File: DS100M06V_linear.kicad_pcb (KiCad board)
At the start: 4 copper layers, 100 x 60 mm, 134 parts, among them J1 wire2board, J10 BNC_panel_mount, J11 wire2board, J2 Wire2Board, J3 wire2board, J4 wire2board, J5 Wire2Board, J6 Wire2Board, J7 Wire2Board, J8 red_safety_4mm_connector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

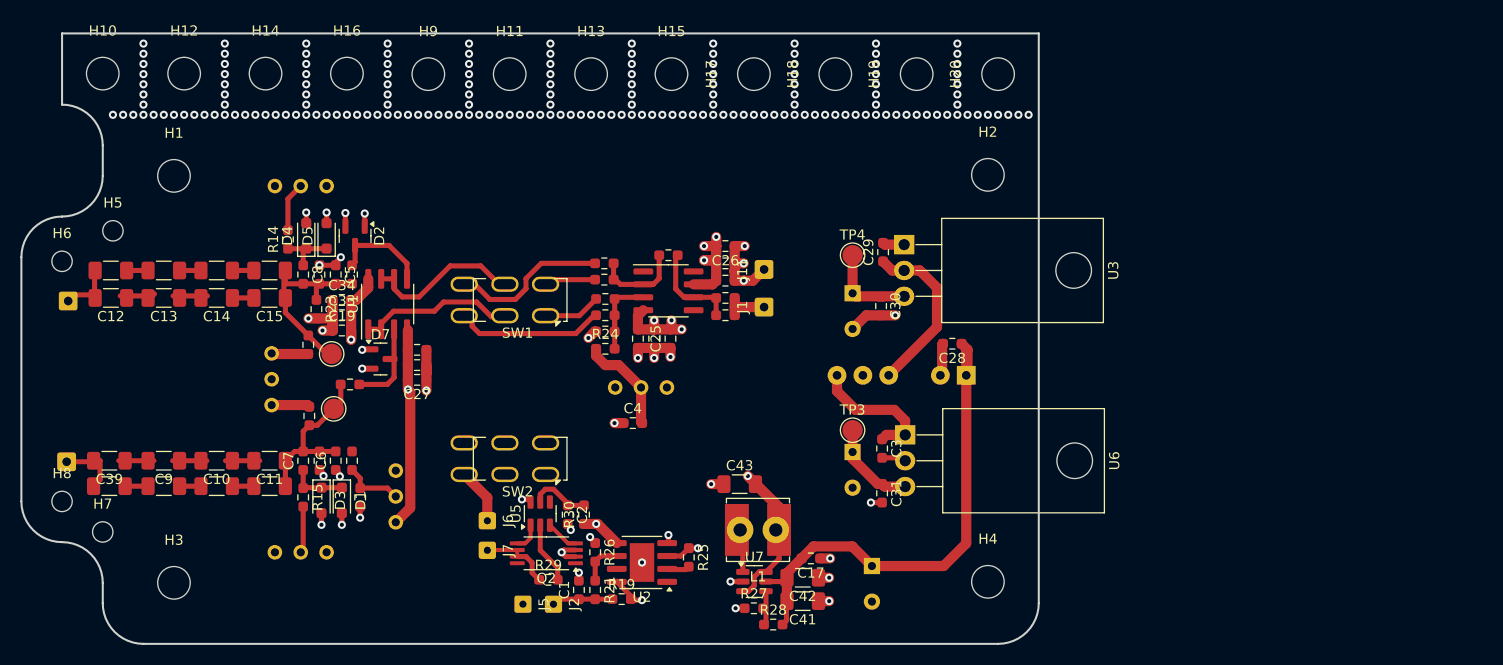
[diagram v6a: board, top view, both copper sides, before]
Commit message: Added capacitance multiplier.
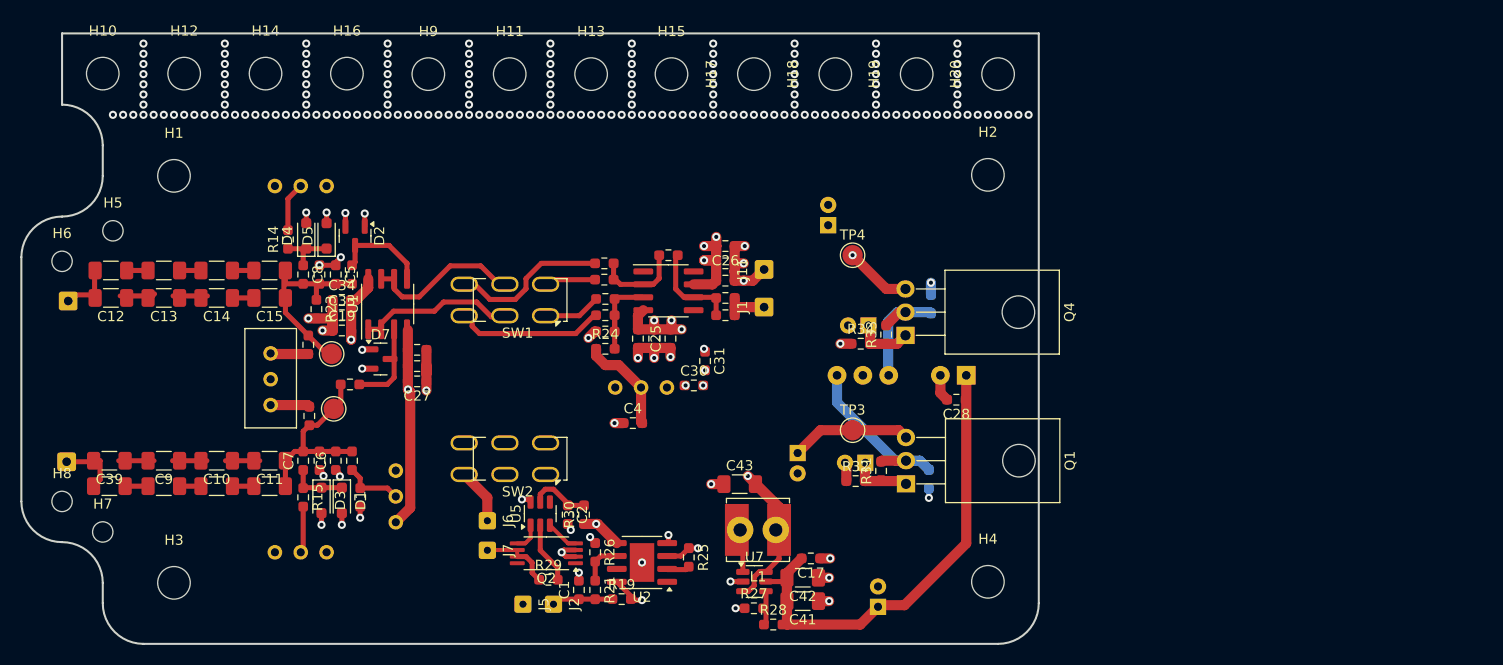
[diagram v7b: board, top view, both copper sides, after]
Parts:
- removed U3: L7905, Package_TO_SOT_THT:TO-220-3_Horizontal_TabDown
- removed U6: L7805, Package_TO_SOT_THT:TO-220-3_Horizontal_TabDown
- added C16: 47u, Capacitor_THT:CP_Radial_D5.0mm_P2.00mm, B.Cu at (168.0, 133.2)
- added C44: 47u, Capacitor_THT:CP_Radial_D5.0mm_P2.00mm, B.Cu at (161.3, 132.2)
- added Q1: BD679, Package_TO_SOT_THT:TO-126-3_Horizontal_TabUp, F.Cu at (171.9, 135.3)
- added Q4: BD680, Package_TO_SOT_THT:TO-126-3_Horizontal_TabUp, F.Cu at (171.9, 120.7)
- added R31: 1k, Resistor_SMD:R_0603_1608Metric_Pad0.98x0.95mm_HandSolder, F.Cu at (169.5, 134.0)
- added R32: 3k3, Resistor_SMD:R_0603_1608Metric_Pad0.98x0.95mm_HandSolder, F.Cu at (167.0, 135.0)
- added R33: 1k, Resistor_SMD:R_0603_1608Metric_Pad0.98x0.95mm_HandSolder, F.Cu at (170.0, 120.6)
- added R34: 3k3, Resistor_SMD:R_0603_1608Metric_Pad0.98x0.95mm_HandSolder, F.Cu at (167.5, 121.5)
- C20, C36, C40: value 470u -> 47u; footprint Capacitor_THT:CP_Radial_D8.0mm_P3.50mm -> Capacitor_THT:CP_Radial_D5.0mm_P2.00mm
- C29, C3: moved to B.Cu
- RV2: moved to F.Cu
- moved C36 22.4 mm to (164.3, 109.9), turned to 90 degrees
- moved C31 21.7 mm to (152.2, 123.2)
- moved C30 20.0 mm to (151.1, 125.6), turned to 0 degrees
- moved C29 6.94 mm to (174.4, 117.6)
- moved C28 5.51 mm to (176.9, 127.0)
- moved C3 5.49 mm to (174.2, 134.8)
- moved C40 4.05 mm to (169.2, 147.4), turned to 90 degrees
- moved C20 3.52 mm to (168.3, 119.7), turned to 180 degrees
- moved C27 0.15 mm to (123.9, 125.2)
- moved RV2 0.14 mm to (109.5, 122.3)
- moved C18 0.10 mm to (123.9, 123.7)
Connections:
- C20 pad 1: -5V -> Net-(Q4-B)
- C36 pad 1: +5V -> -5V
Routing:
- net Net-(Q1-B): track 0.00 -> 5.97 mm
- net Net-(Q4-B): track 0.00 -> 5.70 mm
- net 0: track 52.1 -> 47.3 mm, vias 190 -> 25
- net Net-(PS1--Vout): track 16.9 -> 12.4 mm
- net Net-(PS1-+Vout): track 13.3 -> 17.3 mm
- net +5V: track 156.9 -> 153.2 mm, vias 6 -> 7
- net -5V: track 132.8 -> 129.4 mm, vias 6 -> 8
- net Net-(C11-Pad1): track 16.6 -> 18.8 mm
- net Net-(PS1-+Vin): track 50.2 -> 52.2 mm
- net Earth: track 18.5 -> 18.0 mm
- net (no net): vias 0 -> 168

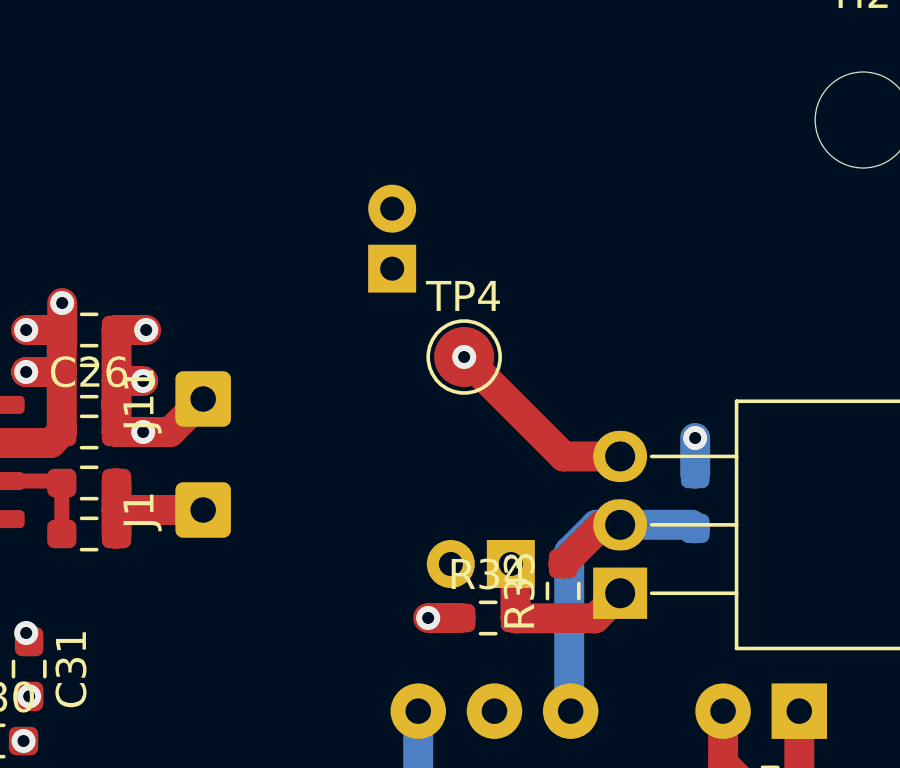
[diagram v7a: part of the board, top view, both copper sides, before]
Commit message: Fixed electrolytics.
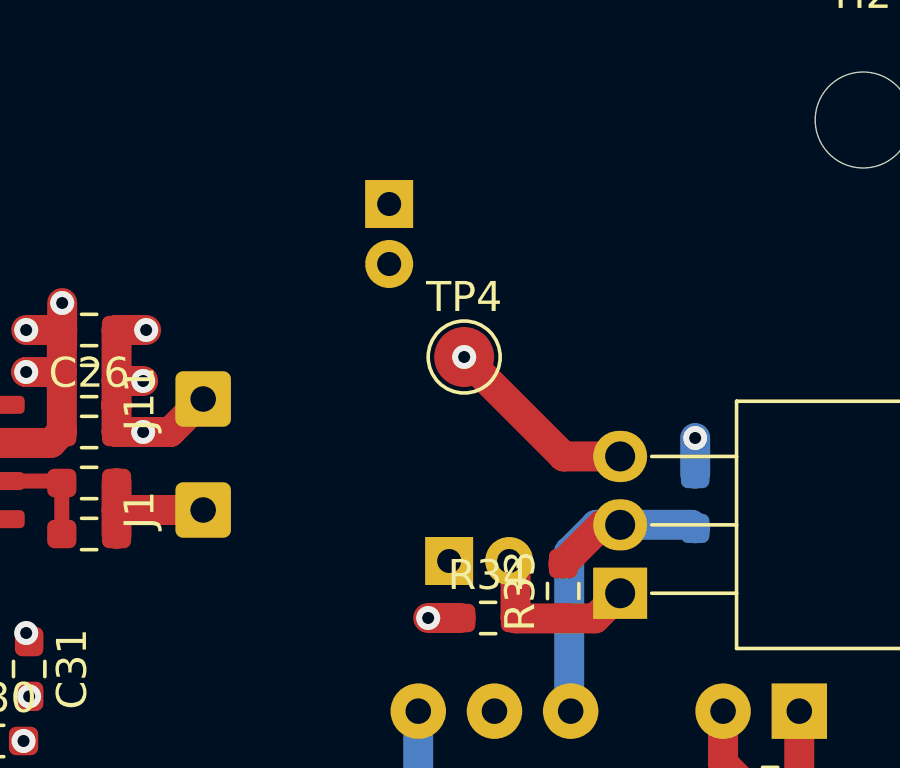
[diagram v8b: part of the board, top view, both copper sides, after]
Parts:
- moved C36 2.16 mm to (164.2, 107.7), turned to -90 degrees
- moved C20 2.06 mm to (166.2, 119.6), turned to 0 degrees
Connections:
- C20 pad 1: Net-(Q4-B) -> 0
- C20 pad 2: 0 -> Net-(Q4-B)
- C36 pad 1: -5V -> 0
- C36 pad 2: 0 -> -5V
